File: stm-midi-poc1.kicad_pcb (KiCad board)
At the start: 4 copper layers, 100 x 100 mm, 116 parts, among them CN1 MIDI Out 1, CN2 MIDI In 1, CN3 MIDI Out 2, CN4 MIDI In 2, CN5 Line out, CN6 Headphone, J1 GT-USB-7010I, J2 SWD, J3 I2C, J4 UART456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

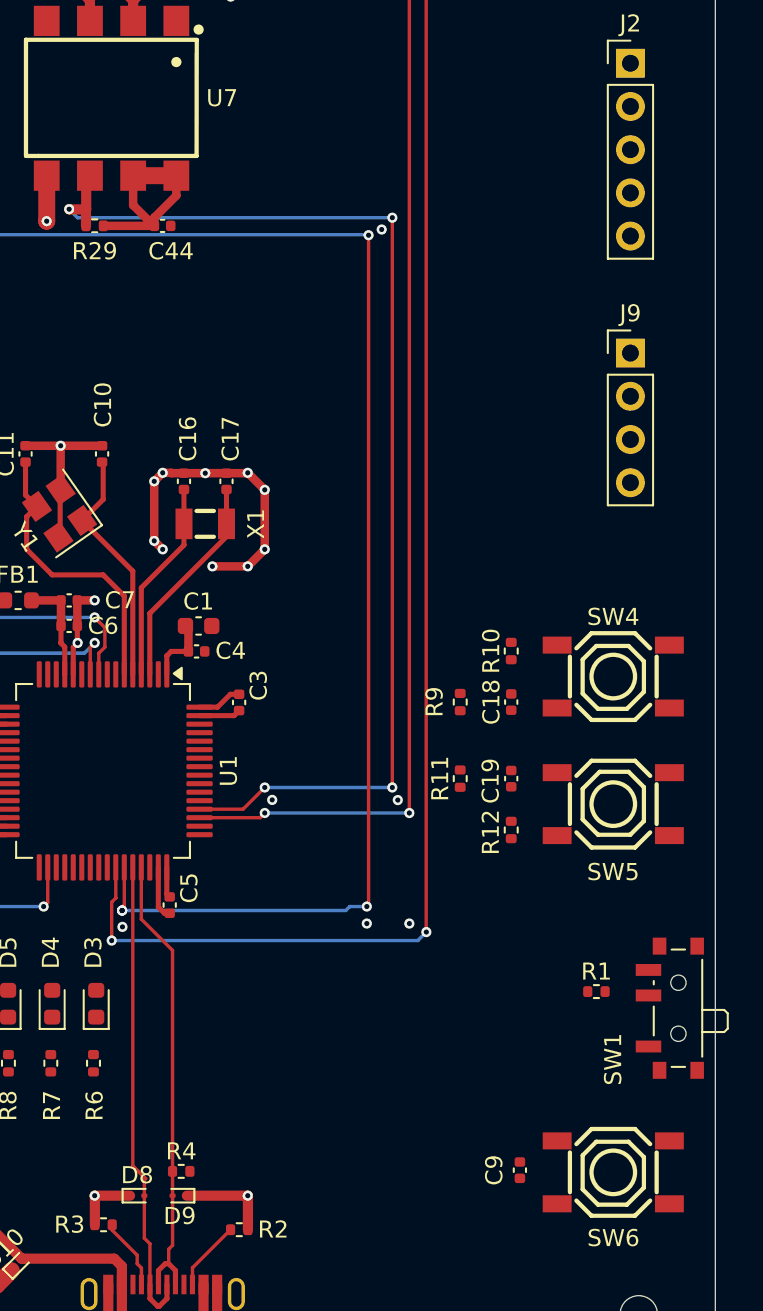
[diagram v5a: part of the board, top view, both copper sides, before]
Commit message: Routed SWD
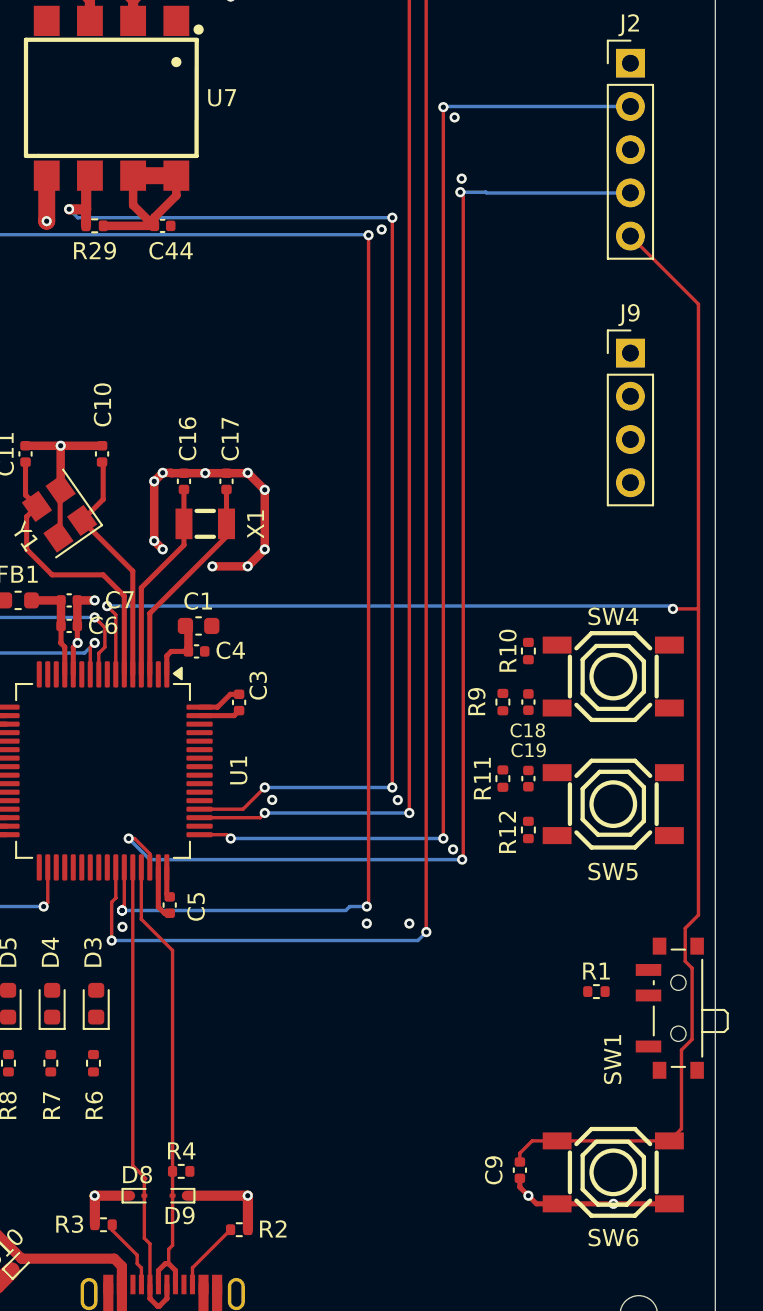
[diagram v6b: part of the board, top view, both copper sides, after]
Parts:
- moved R11 2.51 mm to (194.5, 100.5)
- moved R9 2.51 mm to (194.5, 96.0)
- moved C18 1.01 mm to (196.0, 96.0)
- moved C19 1.01 mm to (196.0, 100.5)
- moved R10 1.01 mm to (196.0, 93.0)
- moved R12 1.01 mm to (196.0, 103.5)
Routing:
- net NRST: track 0.00 -> 104.6 mm, vias 0 -> 2
- net SYS_JTMS-SWDIO: track 0.00 -> 71.9 mm, vias 0 -> 3
- net SYS_JTCK-SWCLK: track 0.00 -> 68.4 mm, vias 0 -> 3
- net GND: track 196.7 -> 206.4 mm, vias 85 -> 90

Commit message: WIP: Routing SPI
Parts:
- moved J3 85.5 mm to (202.0, 83.6)
- moved R20 80.6 mm to (203.5, 87.5), turned to 90 degrees
- moved R19 79.7 mm to (202.0, 87.5), turned to 90 degrees
- moved R18 77.8 mm to (199.5, 87.5), turned to -90 degrees
- moved R17 74.8 mm to (198.0, 87.5), turned to -90 degrees
- moved J9 68.1 mm to (134.5, 66.2)
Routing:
- net +3V3: track 60.0 -> 85.9 mm
- net I2C1_SDA: track 0.00 -> 13.6 mm
- net I2C2_SDA: track 0.00 -> 13.5 mm
- net I2C1_SCL: track 0.00 -> 8.10 mm
- net I2C2_SCL: track 0.00 -> 8.09 mm

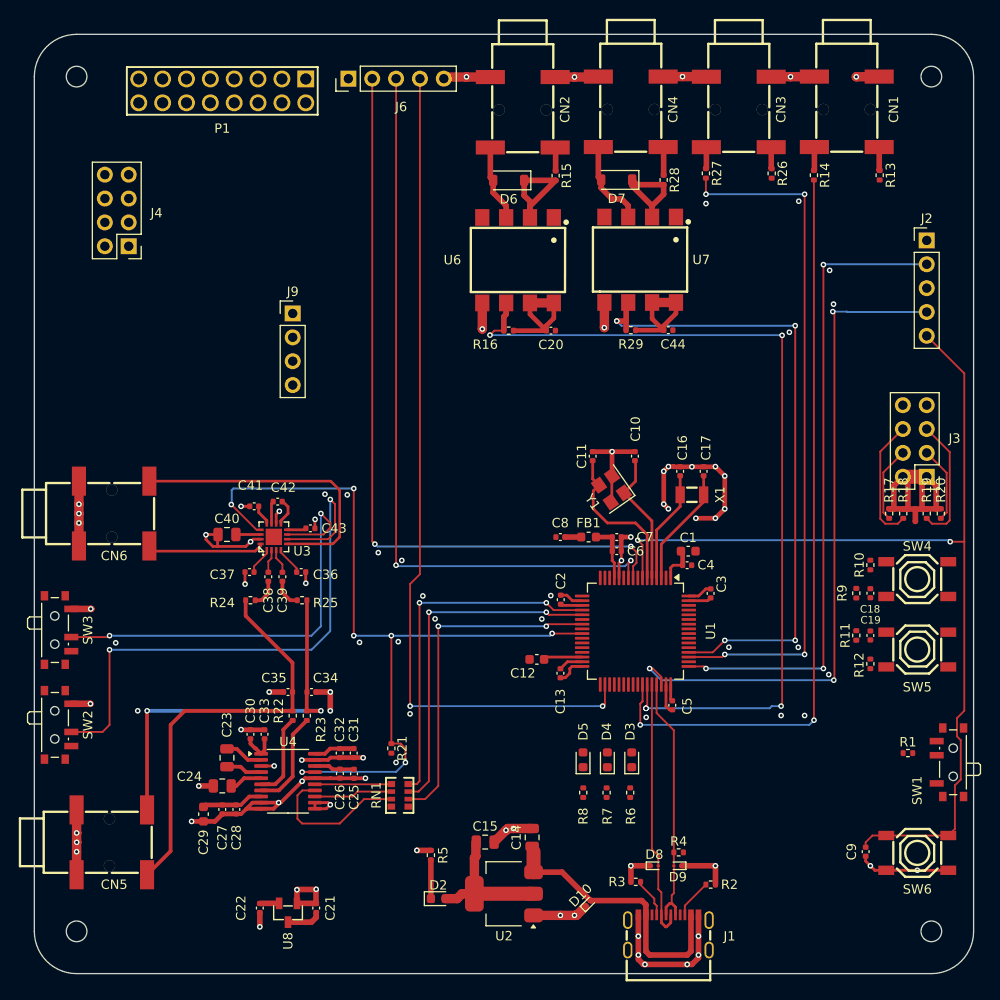
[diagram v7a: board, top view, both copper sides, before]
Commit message: Routed I²C (previous commit was WIP for I²C as well)
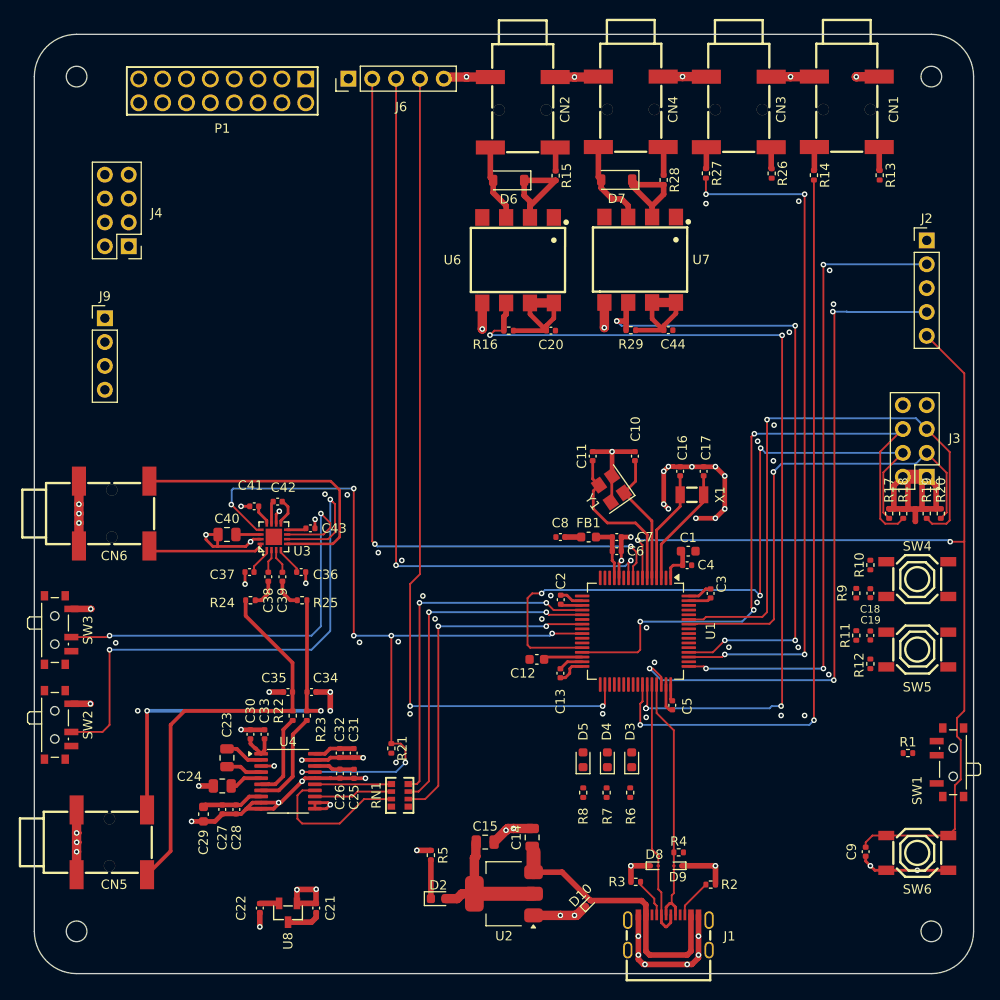
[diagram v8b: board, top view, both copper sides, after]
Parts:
- moved J9 20.0 mm to (114.5, 66.7)
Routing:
- net I2C2_SCL: track 8.09 -> 75.4 mm, vias 0 -> 3
- net I2C2_SDA: track 13.5 -> 70.4 mm, vias 0 -> 3
- net I2C1_SDA: track 13.6 -> 60.3 mm, vias 0 -> 1
- net I2C1_SCL: track 8.10 -> 50.3 mm, vias 0 -> 1
- net GND: vias 90 -> 97
